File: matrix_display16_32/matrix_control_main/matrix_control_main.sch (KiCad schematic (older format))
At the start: 37 parts, among them J1 Conn_01x05_Male, J2 Conn_01x04_Male, P1 Connector_USB_C_Plug_USB2.0, Q1 SOT-23_SS8050_Y1, SW1 RST, SW2 Dowload, U1 ESP-12, U2 CH340E, U3 DS3231, U4 XC6228D332VR-G

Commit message: 修改matrix_display16_32 3D模型封装
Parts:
- D2: footprint lc_lib:0603_LED_S1 -> LED_SMD:LED_0603_1608Metric
- J1: footprint Connector_PinHeader_2.00mm:PinHeader_1x05_P2.00mm_Vertical -> Connector_PinSocket_2.00mm:PinSocket_1x05_P2.00mm_Vertical; symbol Connector:Conn_01x05_Male -> matrix_control_main-rescue:Conn_01x05_Male-Connector
- J2: footprint Connector_PinHeader_2.54mm:PinHeader_1x04_P2.54mm_Vertical -> matrix_control_main:Pin_1x04_P2.54mm_DHT11; symbol Connector:Conn_01x04_Male -> matrix_control_main-rescue:Conn_01x04_Male-Connector
- P1: footprint matrix_control_main:USB-Type-C -> WDebug_DAPLink:USB-Type-C
- SW1, SW2: footprint matrix_control_main:SWITCH_PUSH -> WDebug_DAPLink:SWITCH_PUSH
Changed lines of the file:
@@
 	4450 2200 4450 2450
 $Comp
-L power:GND #PWR0103
+L matrix_control_main-rescue:GND-power #PWR0103
 U 1 1 5E09737A
 P 1750 2400
@@
 F 0 "SW1" H 1250 2350 60  0000 L CNN
 F 1 "RST" V 1403 2552 60  0001 L CNN
-F 2 "matrix_control_main:SWITCH_PUSH" H 1350 3450 60  0001 C CNN
+F 2 "WDebug_DAPLink:SWITCH_PUSH" H 1350 3450 60  0001 C CNN
 F 3 "" H 1070 1975 60  0001 C CNN
 	1    1350 2450
@@
 	1350 2150 1750 2150
 $Comp
-L power:GND #PWR0104
+L matrix_control_main-rescue:GND-power #PWR0104
 U 1 1 5E09B22F
 P 1350 2850
@@
 	1950 2850 2050 2850
 $Comp
-L power:GND #PWR0106
+L matrix_control_main-rescue:GND-power #PWR0106
 U 1 1 5E0A3C38
 P 3750 2950
@@
 	3750 2850 3750 2950
 $Comp
-L Connector:Conn_01x05_Male J1
+L matrix_control_main-rescue:Conn_01x05_Male-Connector J1
 U 1 1 5E0A9DCD
 P 8650 3750
 F 0 "J1" H 8758 4131 50  0000 C CNN
 F 1 "Conn_01x05_Male" H 8758 4040 50  0000 C CNN
-F 2 "Connector_PinHeader_2.00mm:PinHeader_1x05_P2.00mm_Vertical" H 8650 3750 50  0001 C CNN
+F 2 "Connector_PinSocket_2.00mm:PinSocket_1x05_P2.00mm_Vertical" H 8650 3750 50  0001 C CNN
 F 3 "~" H 8650 3750 50  0001 C CNN
 	1    8650 3750
@@
 $EndComp
 $Comp
-L power:+5V #PWR0107
+L matrix_control_main-rescue:+5V-power #PWR0107
 U 1 1 5E0AAD99
 P 9350 3550
@@
 $EndComp
 $Comp
-L power:GND #PWR0108
+L matrix_control_main-rescue:GND-power #PWR0108
 U 1 1 5E0AC6A3
 P 9350 3650
@@
 DIN
 $Comp
-L power:GND #PWR0109
+L matrix_control_main-rescue:GND-power #PWR0109
 U 1 1 5E0B1BB6
 P 3950 3150
@@
 F 0 "SW2" H 4150 2800 60  0000 L CNN
 F 1 "Dowload" V 4303 3002 60  0001 L CNN
-F 2 "matrix_control_main:SWITCH_PUSH" H 4250 3900 60  0001 C CNN
+F 2 "WDebug_DAPLink:SWITCH_PUSH" H 4250 3900 60  0001 C CNN
 F 3 "" H 3970 2425 60  0001 C CNN
 	1    4250 2900
@@
 $EndComp
 $Comp
-L power:GND #PWR0110
+L matrix_control_main-rescue:GND-power #PWR0110
 U 1 1 5E0B7313
 P 4250 3300
@@
 TXD
 $Comp
-L power:+5V #PWR0111
+L matrix_control_main-rescue:+5V-power #PWR0111
 U 1 1 5DD2F874
 P 2700 4050
@@
 $EndComp
 $Comp
-L power:GND #PWR0112
+L matrix_control_main-rescue:GND-power #PWR0112
 U 1 1 5DD30439
 P 2450 5850
@@
 NoConn ~ 2400 4500
 $Comp
-L power:GND #PWR0113
+L matrix_control_main-rescue:GND-power #PWR0113
 U 1 1 5DD3CB38
 P 4500 4700
@@
 $EndComp
 $Comp
-L power:+5V #PWR0114
+L matrix_control_main-rescue:+5V-power #PWR0114
 U 1 1 5DD3DC4D
 P 4450 5300
@@
 $EndComp
 $Comp
-L power:GND #PWR0115
+L matrix_control_main-rescue:GND-power #PWR0115
 U 1 1 5DD2F0ED
 P 6650 2800
@@
 	6650 2650 6650 2800
 $Comp
-L Connector:Conn_01x04_Male J2
+L matrix_control_main-rescue:Conn_01x04_Male-Connector J2
 U 1 1 5DD3613D
 P 8550 2000
 F 0 "J2" H 8658 2281 50  0000 C CNN
 F 1 "Conn_01x04_Male" H 8658 2190 50  0000 C CNN
-F 2 "Connector_PinHeader_2.54mm:PinHeader_1x04_P2.54mm_Vertical" H 8550 2000 50  0001 C CNN
+F 2 "matrix_control_main:Pin_1x04_P2.54mm_DHT11" H 8550 2000 50  0001 C CNN
 F 3 "~" H 8550 2000 50  0001 C CNN
 	1    8550 2000
@@
 $EndComp
 $Comp
-L power:GND #PWR0118
+L matrix_control_main-rescue:GND-power #PWR0118
 U 1 1 5DD3AAA9
 P 9100 2300
@@
 F 0 "P1" H 1907 5667 50  0000 C CNN
 F 1 "Connector_USB_C_Plug_USB2.0" H 1907 5576 50  0000 C CNN
-F 2 "matrix_control_main:USB-Type-C" H 1950 4800 50  0001 C CNN
+F 2 "WDebug_DAPLink:USB-Type-C" H 1950 4800 50  0001 C CNN
 F 3 "" H 1950 4800 50  0001 C CNN
 	1    1800 4800
@@
 $EndComp
 $Comp
-L power:+5V #PWR0122
+L matrix_control_main-rescue:+5V-power #PWR0122
 U 1 1 5DD6DC93
 P 2150 7200
@@
 $EndComp
 $Comp
-L power:+5V #PWR0121
+L matrix_control_main-rescue:+5V-power #PWR0121
 U 1 1 5DD6CBBD
 P 1650 6450
@@
 $EndComp
 $Comp
-L power:GND #PWR0120
+L matrix_control_main-rescue:GND-power #PWR0120
 U 1 1 5DD6C67B
 P 4000 7000
@@
 $EndComp
 $Comp
-L power:GND #PWR0119
+L matrix_control_main-rescue:GND-power #PWR0119
 U 1 1 5DD6A118
 P 1650 7000
@@
 $EndComp
 $Comp
-L power:+5V #PWR0124
+L matrix_control_main-rescue:+5V-power #PWR0124
 U 1 1 5DEB80A3
 P 7600 4350
@@
 $EndComp
 $Comp
-L power:GND #PWR0125
+L matrix_control_main-rescue:GND-power #PWR0125
 U 1 1 5DEB8ABE
 P 7600 5850
@@
 F 0 "D2" H 5450 1233 50  0000 C CNN
 F 1 "0603_绿灯" H 4949 1860 50  0001 L BNN
-F 2 "lc_lib:0603_LED_S1" H 4899 1200 50  0001 L BNN
+F 2 "LED_SMD:LED_0603_1608Metric" H 4899 1200 50  0001 L BNN
 F 3 "http://www.szlcsc.com/product/details_73152.html" H 4899 1300 50  0001 L BNN
 F 4 "发光二极管" H 4900 1600 50  0001 C CNN "description"

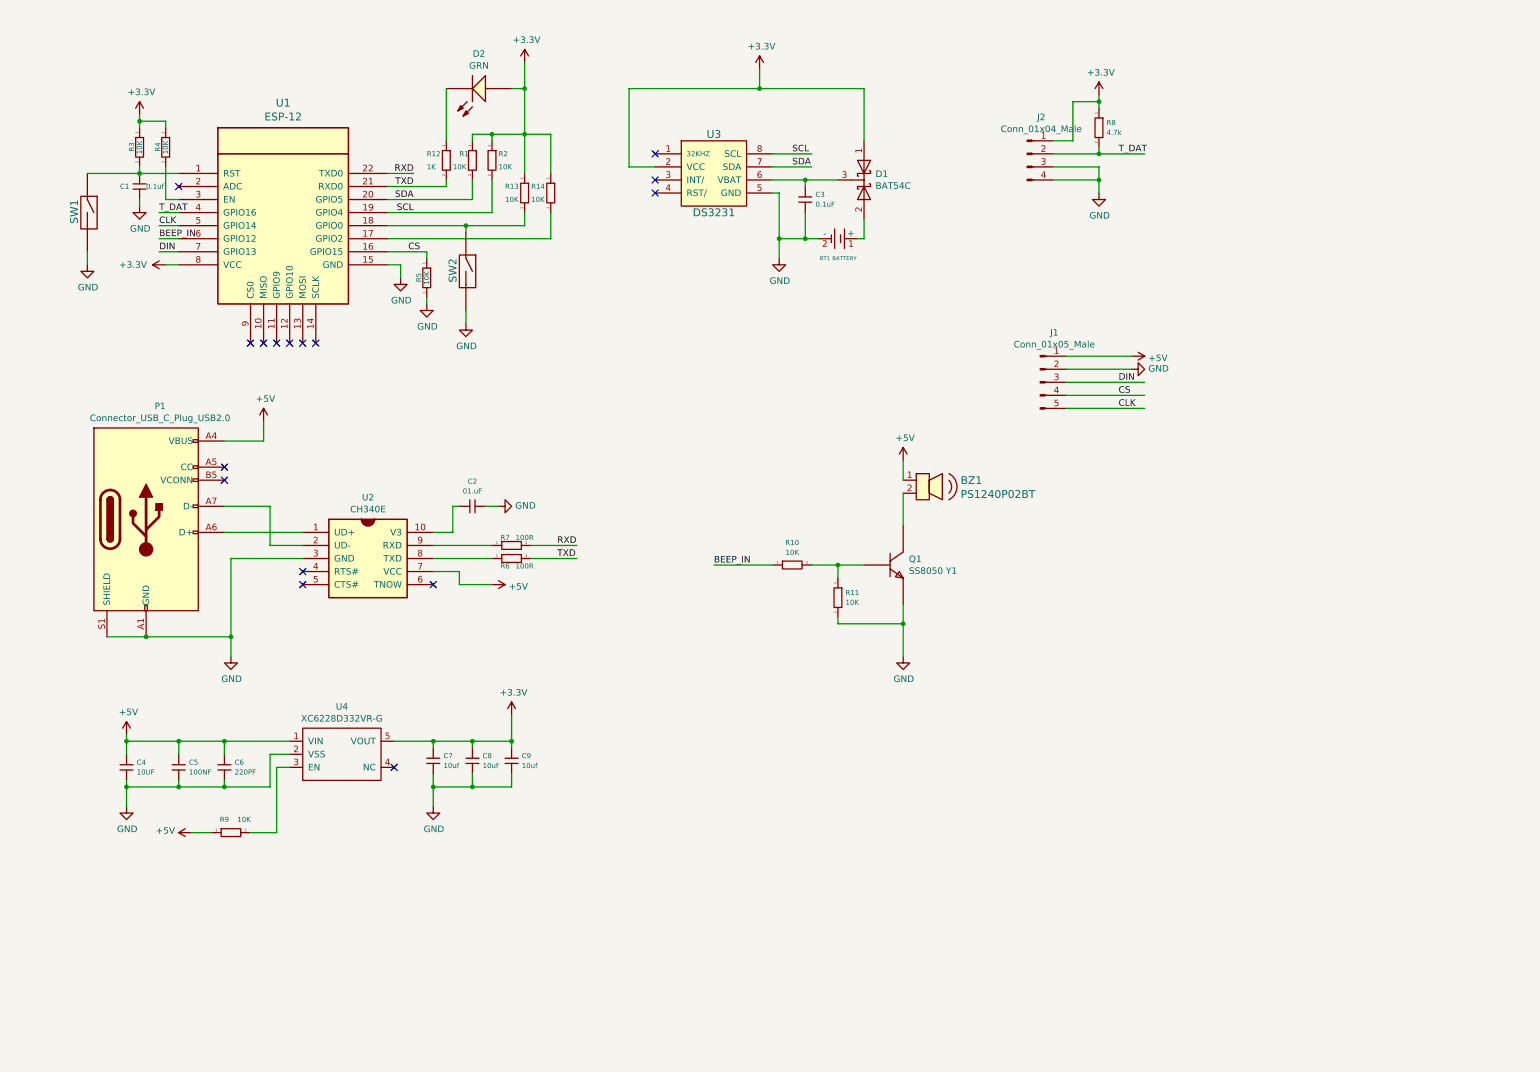
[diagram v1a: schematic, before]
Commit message: 修改点阵铜柱洞3.5MM 修改连接接口2.54MM
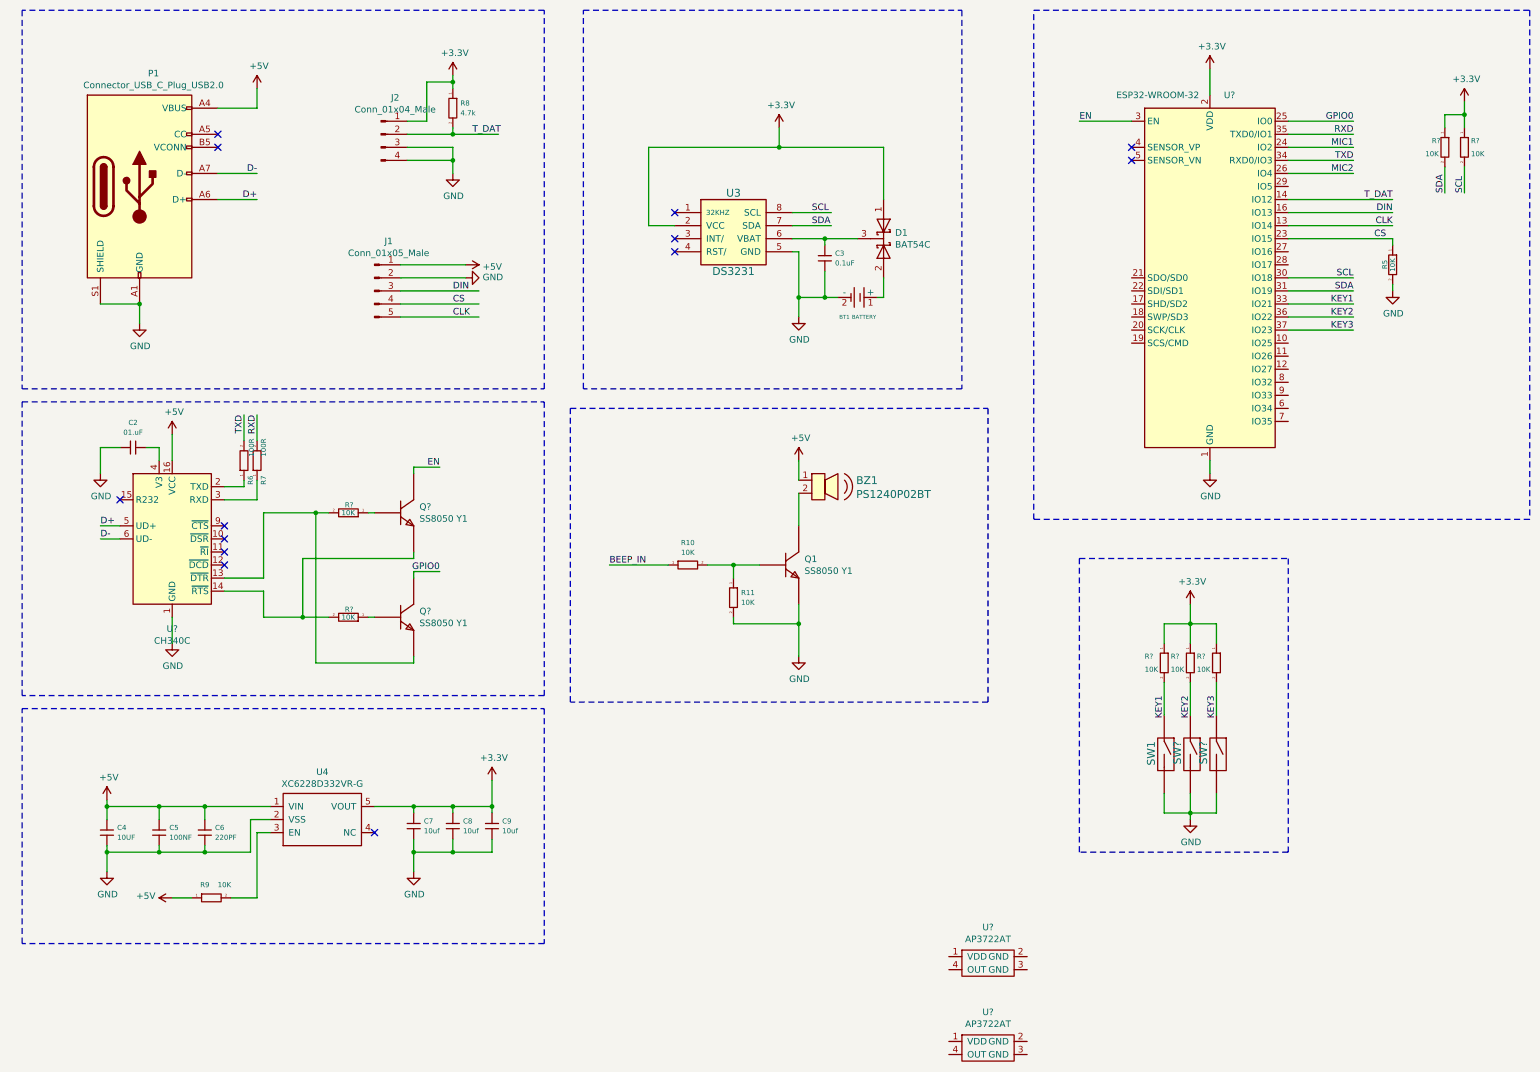
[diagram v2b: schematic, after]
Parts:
- removed C1: 0.1uf, matrix_control_main:0603_C, symbol matrix_control_main-rescue:C(MM)-LibCool-matrix_display-rescue
- removed D2: 0603_绿灯, LED_SMD:LED_0603_1608Metric, symbol matrix_control_main-rescue:0603_绿灯-LC_led
- removed R1, R13, R14, R2, R3, R4: 10K, matrix_control_main:0603_R, symbol matrix_control_main-rescue:RES(M)-LibCool-matrix_display-rescue
- removed R12: 1K, matrix_control_main:0603_R, symbol matrix_control_main-rescue:RES(M)-LibCool-hack_clock-rescue
- removed SW2: Dowload, WDebug_DAPLink:SWITCH_PUSH, symbol matrix_control_main-rescue:switch-LibCool-hack_clock-rescue
- removed U1: ESP-12, matrix_control_main:ESP-12E, symbol matrix_control_main-rescue:ESP-12-LibCool-hack_clock-rescue
- removed U2: CH340E, matrix_control_main:TSSOP-10_3x3mm_P0.5mm, symbol matrix_control_main-rescue:CH340E-LibCool-hack_clock-rescue
- added Q? (x2): SOT-23_SS8050_Y1-lc_Transistor_NPN, lc_lib:SOT-23(SOT-23-3), symbol matrix_control_main-rescue:SOT-23_SS8050_Y1-lc_Transistor_NPN
- added R? (x7): 10K, matrix_control_main:0603_R, symbol matrix_control_main-rescue:RES(M)-LibCool-matrix_display-rescue
- added SW? (x2): RST, WDebug_DAPLink:SWITCH_PUSH, symbol matrix_control_main-rescue:switch-LibCool-hack_clock-rescue
- added U?: CH340C, Package_SO:SOIC-16_3.9x9.9mm_P1.27mm, symbol Interface_USB:CH340C
- added U?: ESP32-WROOM-32, RF_Module:ESP32-WROOM-32, symbol RF_Module:ESP32-WROOM-32
- added U? (x2): AP3722AT, symbol WeissLib:AP3722AT
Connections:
- net labels added: D+, D-, EN, GPIO0, KEY1, KEY2, KEY3, MIC1, MIC2
- wire segments 147 -> 159
- no-connect marks 16 -> 13
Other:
- moved on the sheet: BT1, BZ1, C2, C3, C4, C5, C6, C7, C8, C9, D1, J1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

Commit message: 修改matrixDisplay1632控制版
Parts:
- U? (x2): symbol WeissLib:AP3722AT -> matrix_control_main-rescue:AP3722AT-WeissLib
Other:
- moved on the sheet: BT1, C3, D1, R?, SW1, SW?, U3, U?
